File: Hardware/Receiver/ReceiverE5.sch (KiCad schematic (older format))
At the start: 37 parts, among them J1 KBUS, J2 AVR-PDI-6A, J3 CONN_01X08, J4 CONN_01X06, J5 CONN_01X06, J6 CONN_01X04, J7 CONN_01X04, U1 ATXMEGA32E5-A, U2 LM2731, U3 SN74LV07A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

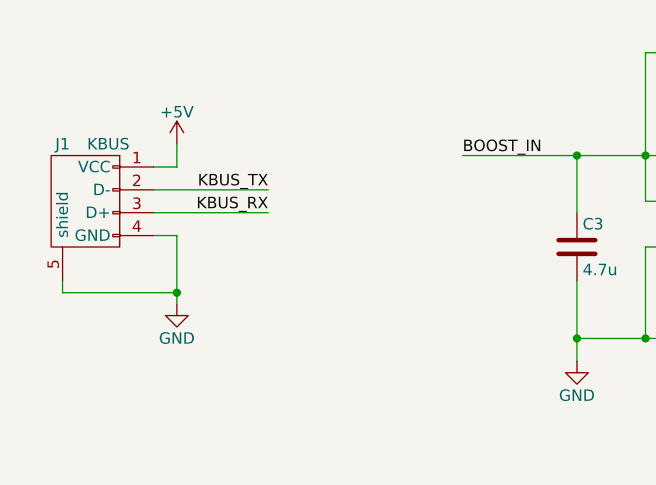
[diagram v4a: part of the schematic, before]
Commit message: Added missing series termination resistors for KBUS
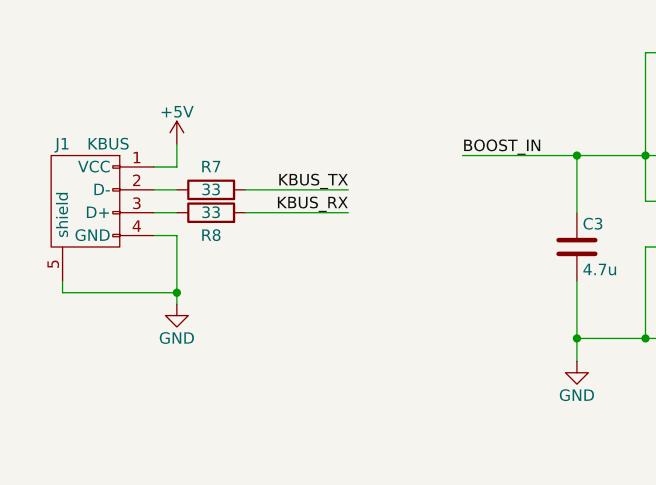
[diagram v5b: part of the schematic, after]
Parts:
- added R7, R8: 33, Resistors_SMD:R_0603, symbol R
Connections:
- net KBUS_RX: now also R8.2; no longer J1.3 (D+)
- net KBUS_TX: now also R7.2; no longer J1.2 (D-)
- new net: J1.2 (D-), R7.1
- new net: J1.3 (D+), R8.1
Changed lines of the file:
@@
 $EndComp
 $Comp
-L +5V #PWR01
+L +5V #PWR12
 U 1 1 582469D6
 P 6100 1150
-F 0 "#PWR01" H 6100 1000 50  0001 C CNN
+F 0 "#PWR12" H 6100 1000 50  0001 C CNN
 F 1 "+5V" H 6100 1290 50  0000 C CNN
 F 2 "" H 6100 1150 50  0000 C CNN
@@
 $EndComp
 $Comp
-L GND #PWR02
+L GND #PWR7
 U 1 1 582469FA
 P 3100 2150
-F 0 "#PWR02" H 3100 1900 50  0001 C CNN
+F 0 "#PWR7" H 3100 1900 50  0001 C CNN
 F 1 "GND" H 3100 2000 50  0000 C CNN
 F 2 "" H 3100 2150 50  0000 C CNN
@@
 $EndComp
 $Comp
-L PWR_FLAG #FLG03
+L PWR_FLAG #FLG1
 U 1 1 58246A8F
 P 10700 1350
-F 0 "#FLG03" H 10700 1445 50  0001 C CNN
+F 0 "#FLG1" H 10700 1445 50  0001 C CNN
 F 1 "PWR_FLAG" H 10700 1530 50  0000 C CNN
 F 2 "" H 10700 1350 50  0000 C CNN
@@
 $EndComp
 $Comp
-L +5V #PWR04
+L +5V #PWR32
 U 1 1 58246B44
 P 10350 1350
-F 0 "#PWR04" H 10350 1200 50  0001 C CNN
+F 0 "#PWR32" H 10350 1200 50  0001 C CNN
 F 1 "+5V" H 10350 1490 50  0000 C CNN
 F 2 "" H 10350 1350 50  0000 C CNN
@@
 $EndComp
 $Comp
-L +5V #PWR05
+L +5V #PWR5
 U 1 1 5824886A
 P 1350 1200
-F 0 "#PWR05" H 1350 1050 50  0001 C CNN
+F 0 "#PWR5" H 1350 1050 50  0001 C CNN
 F 1 "+5V" H 1350 1340 50  0000 C CNN
 F 2 "" H 1350 1200 50  0000 C CNN
@@
 $EndComp
 $Comp
-L GND #PWR06
+L GND #PWR6
 U 1 1 582489D4
 P 1350 1900
-F 0 "#PWR06" H 1350 1650 50  0001 C CNN
+F 0 "#PWR6" H 1350 1650 50  0001 C CNN
 F 1 "GND" H 1350 1750 50  0000 C CNN
 F 2 "" H 1350 1900 50  0000 C CNN
@@
 $EndComp
 $Comp
-L +5V #PWR07
+L +5V #PWR15
 U 1 1 5824ABA7
 P 6700 1300
-F 0 "#PWR07" H 6700 1150 50  0001 C CNN
+F 0 "#PWR15" H 6700 1150 50  0001 C CNN
 F 1 "+5V" H 6700 1440 50  0000 C CNN
 F 2 "" H 6700 1300 50  0000 C CNN
@@
 $EndComp
 $Comp
-L GND #PWR08
+L GND #PWR16
 U 1 1 5824AD24
 P 6700 1700
-F 0 "#PWR08" H 6700 1450 50  0001 C CNN
+F 0 "#PWR16" H 6700 1450 50  0001 C CNN
 F 1 "GND" H 6700 1550 50  0000 C CNN
 F 2 "" H 6700 1700 50  0000 C CNN
@@
 $EndComp
 $Comp
-L GND #PWR09
+L GND #PWR20
 U 1 1 5824B020
 P 7950 1700
-F 0 "#PWR09" H 7950 1450 50  0001 C CNN
+F 0 "#PWR20" H 7950 1450 50  0001 C CNN
 F 1 "GND" H 7950 1550 50  0000 C CNN
 F 2 "" H 7950 1700 50  0000 C CNN
@@
 $EndComp
 $Comp
-L +3.3V #PWR010
+L +3.3V #PWR19
 U 1 1 5824B213
 P 7950 1300
-F 0 "#PWR010" H 7950 1150 50  0001 C CNN
+F 0 "#PWR19" H 7950 1150 50  0001 C CNN
 F 1 "+3.3V" H 7950 1440 50  0000 C CNN
 F 2 "" H 7950 1300 50  0000 C CNN
@@
 $EndComp
 $Comp
-L +3.3V #PWR011
+L +3.3V #PWR33
 U 1 1 5824C026
 P 10350 1650
-F 0 "#PWR011" H 10350 1500 50  0001 C CNN
+F 0 "#PWR33" H 10350 1500 50  0001 C CNN
 F 1 "+3.3V" H 10350 1790 50  0000 C CNN
 F 2 "" H 10350 1650 50  0000 C CNN
@@
 $EndComp
 $Comp
-L PWR_FLAG #FLG012
+L PWR_FLAG #FLG2
 U 1 1 5824C328
 P 10700 1650
-F 0 "#FLG012" H 10700 1745 50  0001 C CNN
+F 0 "#FLG2" H 10700 1745 50  0001 C CNN
 F 1 "PWR_FLAG" H 10700 1830 50  0000 C CNN
 F 2 "" H 10700 1650 50  0000 C CNN
@@
 $EndComp
 $Comp
-L GND #PWR013
+L GND #PWR13
 U 1 1 5824EEE6
 P 6350 4400
-F 0 "#PWR013" H 6350 4150 50  0001 C CNN
+F 0 "#PWR13" H 6350 4150 50  0001 C CNN
 F 1 "GND" H 6350 4250 50  0000 C CNN
 F 2 "" H 6350 4400 50  0000 C CNN
@@
 $EndComp
 $Comp
-L GND #PWR014
+L GND #PWR14
 U 1 1 5824F2F5
 P 6350 5350
-F 0 "#PWR014" H 6350 5100 50  0001 C CNN
+F 0 "#PWR14" H 6350 5100 50  0001 C CNN
 F 1 "GND" H 6350 5200 50  0000 C CNN
 F 2 "" H 6350 5350 50  0000 C CNN
@@
 C5
 $Comp
-L GND #PWR015
+L GND #PWR22
 U 1 1 58251C44
 P 8600 4100
-F 0 "#PWR015" H 8600 3850 50  0001 C CNN
+F 0 "#PWR22" H 8600 3850 50  0001 C CNN
 F 1 "GND" H 8600 3950 50  0000 C CNN
 F 2 "" H 8600 4100 50  0000 C CNN
@@
 $EndComp
 $Comp
-L GND #PWR016
+L GND #PWR24
 U 1 1 58251C82
 P 8600 5000
-F 0 "#PWR016" H 8600 4750 50  0001 C CNN
+F 0 "#PWR24" H 8600 4750 50  0001 C CNN
 F 1 "GND" H 8600 4850 50  0000 C CNN
 F 2 "" H 8600 5000 50  0000 C CNN
@@
 $EndComp
 $Comp
-L +3.3V #PWR017
+L +3.3V #PWR21
 U 1 1 582523F9
 P 8600 3700
-F 0 "#PWR017" H 8600 3550 50  0001 C CNN
+F 0 "#PWR21" H 8600 3550 50  0001 C CNN
 F 1 "+3.3V" H 8600 3840 50  0000 C CNN
 F 2 "" H 8600 3700 50  0000 C CNN
@@
 $EndComp
 $Comp
-L +3.3V #PWR018
+L +3.3V #PWR23
 U 1 1 58252575
 P 8600 4600
-F 0 "#PWR018" H 8600 4450 50  0001 C CNN
+F 0 "#PWR23" H 8600 4450 50  0001 C CNN
 F 1 "+3.3V" H 8600 4740 50  0000 C CNN
 F 2 "" H 8600 4600 50  0000 C CNN
@@
 $EndComp
 $Comp
-L +5V #PWR019
+L +5V #PWR27
 U 1 1 58253B37
 P 9600 3700
-F 0 "#PWR019" H 9600 3550 50  0001 C CNN
+F 0 "#PWR27" H 9600 3550 50  0001 C CNN
 F 1 "+5V" H 9600 3840 50  0000 C CNN
 F 2 "" H 9600 3700 50  0000 C CNN
@@
 $EndComp
 $Comp
-L GND #PWR020
+L GND #PWR29
 U 1 1 58254196
 P 9600 5000
-F 0 "#PWR020" H 9600 4750 50  0001 C CNN
+F 0 "#PWR29" H 9600 4750 50  0001 C CNN
 F 1 "GND" H 9600 4850 50  0000 C CNN
 F 2 "" H 9600 5000 50  0000 C CNN
@@
 $EndComp
 $Comp
-L +5V #PWR021
+L +5V #PWR28
 U 1 1 582542A3
 P 9600 4600
-F 0 "#PWR021" H 9600 4450 50  0001 C CNN
+F 0 "#PWR28" H 9600 4450 50  0001 C CNN
 F 1 "+5V" H 9600 4740 50  0000 C CNN
 F 2 "" H 9600 4600 50  0000 C CNN
@@
 $EndComp
 $Comp
-L +3.3V #PWR022
+L +3.3V #PWR18
 U 1 1 5825A872
 P 7500 4550
-F 0 "#PWR022" H 7500 4400 50  0001 C CNN
+F 0 "#PWR18" H 7500 4400 50  0001 C CNN
 F 1 "+3.3V" H 7500 4690 50  0000 C CNN
 F 2 "" H 7500 4550 50  0000 C CNN
@@
 $EndComp
 $Comp
-L +3.3V #PWR023
+L +3.3V #PWR17
 U 1 1 5825A961
 P 7200 5600
-F 0 "#PWR023" H 7200 5450 50  0001 C CNN
+F 0 "#PWR17" H 7200 5450 50  0001 C CNN
 F 1 "+3.3V" H 7200 5740 50  0000 C CNN
 F 2 "" H 7200 5600 50  0000 C CNN
@@
 $EndComp
 $Comp
-L +5V #PWR024
+L +5V #PWR30
 U 1 1 5825BCEC
 P 10300 5500
-F 0 "#PWR024" H 10300 5350 50  0001 C CNN
+F 0 "#PWR30" H 10300 5350 50  0001 C CNN
 F 1 "+5V" H 10300 5640 50  0000 C CNN
 F 2 "" H 10300 5500 50  0000 C CNN
@@
 $EndComp
 $Comp
-L GND #PWR025
+L GND #PWR31
 U 1 1 5825BEA2
 P 10300 5900
-F 0 "#PWR025" H 10300 5650 50  0001 C CNN
+F 0 "#PWR31" H 10300 5650 50  0001 C CNN
 F 1 "GND" H 10300 5750 50  0000 C CNN
 F 2 "" H 10300 5900 50  0000 C CNN
@@
 	1    0    0    -1
 $EndComp
-Text Label 1750 1400 2    50   ~ 0
+Text Label 2100 1400 2    50   ~ 0
 KBUS_TX
-Text Label 1750 1500 2    50   ~ 0
+Text Label 2100 1500 2    50   ~ 0
 KBUS_RX
 $Comp
@@
 $EndComp
 $Comp
-L GND #PWR026
+L GND #PWR1
 U 1 1 5825FD90
 P 750 5000
-F 0 "#PWR026" H 750 4750 50  0001 C CNN
+F 0 "#PWR1" H 750 4750 50  0001 C CNN
 F 1 "GND" H 750 4850 50  0000 C CNN
 F 2 "" H 750 5000 50  0000 C CNN
@@
 $EndComp
 $Comp
-L GND #PWR027
+L GND #PWR3
 U 1 1 582615C7
 P 1100 3650
-F 0 "#PWR027" H 1100 3400 50  0001 C CNN
+F 0 "#PWR3" H 1100 3400 50  0001 C CNN
 F 1 "GND" H 1100 3500 50  0000 C CNN
 F 2 "" H 1100 3650 50  0000 C CNN
@@
 $EndComp
 $Comp
-L +3.3V #PWR028
+L +3.3V #PWR2
 U 1 1 582618AA
 P 900 3800
-F 0 "#PWR028" H 900 3650 50  0001 C CNN
+F 0 "#PWR2" H 900 3650 50  0001 C CNN
 F 1 "+3.3V" H 900 3940 50  0000 C CNN
 F 2 "" H 900 3800 50  0000 C CNN
@@
 $EndComp
 $Comp
-L +3.3V #PWR029
+L +3.3V #PWR8
 U 1 1 58261F69
 P 3600 2800
-F 0 "#PWR029" H 3600 2650 50  0001 C CNN
+F 0 "#PWR8" H 3600 2650 50  0001 C CNN
 F 1 "+3.3V" H 3600 2940 50  0000 C CNN
 F 2 "" H 3600 2800 50  0000 C CNN
@@
 $EndComp
 $Comp
-L GND #PWR030
+L GND #PWR9
 U 1 1 582625C0
 P 3800 3250
-F 0 "#PWR030" H 3800 3000 50  0001 C CNN
+F 0 "#PWR9" H 3800 3000 50  0001 C CNN
 F 1 "GND" H 3800 3100 50  0000 C CNN
 F 2 "" H 3800 3250 50  0000 C CNN
@@
 $EndComp
 $Comp
-L GND #PWR031
+L GND #PWR11
 U 1 1 58262CE9
 P 4300 3250
-F 0 "#PWR031" H 4300 3000 50  0001 C CNN
+F 0 "#PWR11" H 4300 3000 50  0001 C CNN
 F 1 "GND" H 4300 3100 50  0000 C CNN
 F 2 "" H 4300 3250 50  0000 C CNN
@@
 $EndComp
 $Comp
-L GND #PWR032
+L GND #PWR10
 U 1 1 58264117
 P 3850 5800
-F 0 "#PWR032" H 3850 5550 50  0001 C CNN
+F 0 "#PWR10" H 3850 5550 50  0001 C CNN
 F 1 "GND" H 3850 5650 50  0000 C CNN
 F 2 "" H 3850 5800 50  0000 C CNN
@@
 OPT2
 $Comp
-L GND #PWR033
+L GND #PWR4
 U 1 1 582674C6
 P 1300 6800
-F 0 "#PWR033" H 1300 6550 50  0001 C CNN
+F 0 "#PWR4" H 1300 6550 50  0001 C CNN
 F 1 "GND" H 1300 6650 50  0000 C CNN
 F 2 "" H 1300 6800 50  0000 C CNN
@@
 Wire Wire Line
 	10450 5850 10300 5850
-Wire Wire Line
-	1250 1400 1750 1400
-Wire Wire Line
-	1750 1500 1250 1500
 Wire Wire Line
 	1250 4450 2500 4450
@@
 Connection ~ 6100 1250
 $Comp
-L +3.3V #PWR034
+L +3.3V #PWR25
 U 1 1 5827EBCB
 P 8700 1200
-F 0 "#PWR034" H 8700 1050 50  0001 C CNN
+F 0 "#PWR25" H 8700 1050 50  0001 C CNN
 F 1 "+3.3V" H 8700 1340 50  0000 C CNN
 F 2 "" H 8700 1200 50  0000 C CNN
@@
 Connection ~ 9000 1650
 $Comp
-L GND #PWR035
+L GND #PWR26
 U 1 1 5827F399
 P 8700 1700
-F 0 "#PWR035" H 8700 1450 50  0001 C CNN
+F 0 "#PWR26" H 8700 1450 50  0001 C CNN
 F 1 "GND" H 8700 1550 50  0000 C CNN
 F 2 "" H 8700 1700 50  0000 C CNN
@@
 NoConn ~ 2500 5250
 $Comp
-L PWR_FLAG #FLG036
+L PWR_FLAG #FLG3
 U 1 1 582B30DF
 P 10700 1950
-F 0 "#FLG036" H 10700 2045 50  0001 C CNN
+F 0 "#FLG3" H 10700 2045 50  0001 C CNN
 F 1 "PWR_FLAG" H 10700 2130 50  0000 C CNN
 F 2 "" H 10700 1950 50  0000 C CNN
@@
 $EndComp
 $Comp
-L GND #PWR037
+L GND #PWR34
 U 1 1 582B3159
 P 10700 2000
-F 0 "#PWR037" H 10700 1750 50  0001 C CNN
+F 0 "#PWR34" H 10700 1750 50  0001 C CNN
 F 1 "GND" H 10700 1850 50  0000 C CNN
 F 2 "" H 10700 2000 50  0000 C CNN
@@
 Wire Wire Line
 	10700 2000 10700 1950
+$Comp
+L R R7
+U 1 1 582BC7E3
+P 1500 1400
+F 0 "R7" V 1600 1400 50  0000 C CNN
+F 1 "33" V 1500 1400 50  0000 C CNN
+F 2 "Resistors_SMD:R_0603" V 1430 1400 50  0001 C CNN
+F 3 "" H 1500 1400 50  0000 C CNN
+	1    1500 1400
+	0    -1   -1   0
+$EndComp
+$Comp
+L R R8
+U 1 1 582BEB1F
+P 1500 1500
+F 0 "R8" V 1400 1500 50  0000 C CNN
+F 1 "33" V 1500 1500 50  0000 C CNN
+F 2 "Resistors_SMD:R_0603" V 1430 1500 50  0001 C CNN
+F 3 "" H 1500 1500 50  0000 C CNN
+	1    1500 1500
+	0    -1   -1   0
+$EndComp
+Wire Wire Line
+	2100 1400 1650 1400
+Wire Wire Line
+	1650 1500 2100 1500
+Wire Wire Line
+	1350 1400 1250 1400
+Wire Wire Line
+	1250 1500 1350 1500
 $EndSCHEMATC
